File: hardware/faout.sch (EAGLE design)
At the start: 159 parts, among them IC2 MT48LC8M16A2, P1 TE_CONN_MTE_HEADER3R, Q1 L7812CD2T-TR, Q2 L7912CD2T-TR, Q3 12MHz, Q4 ASFL, U1 LM3671MF-3.3, U10 REF102AU, U11 OPA4277UA, U12 DAC8812, U13 REF102AU, U14 OPA4277UA, U15 DAC8812, U16 LM7321MF, U2 LM3671MF-1.2, U3 93LC46BT-I/OT, U4 6SLX9TQG144, U5 M25PE16SO8N, U7 REF102AU, U8 OPA4277UA, U9 DAC8812

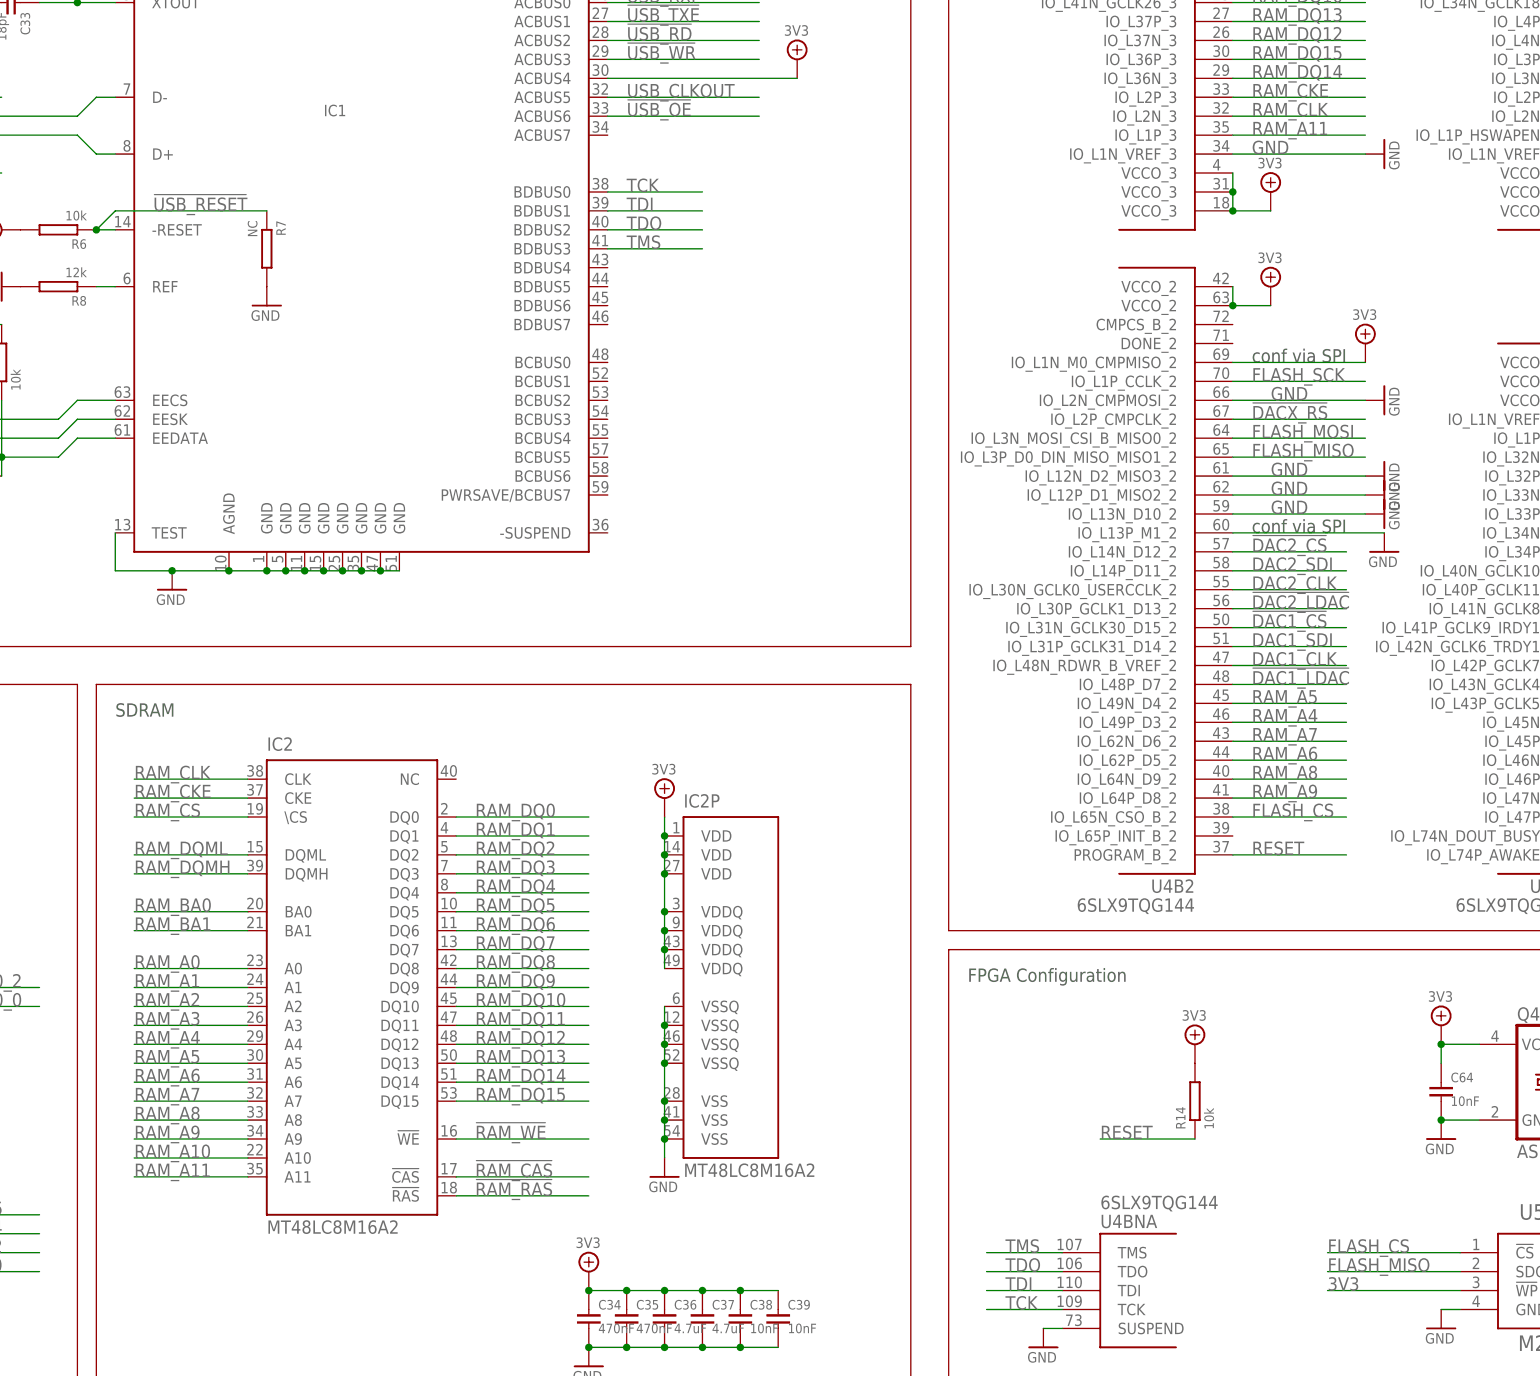
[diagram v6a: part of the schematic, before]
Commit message: Modify board for 256Mbit DRAM (MT48LC16M16) compatibility.
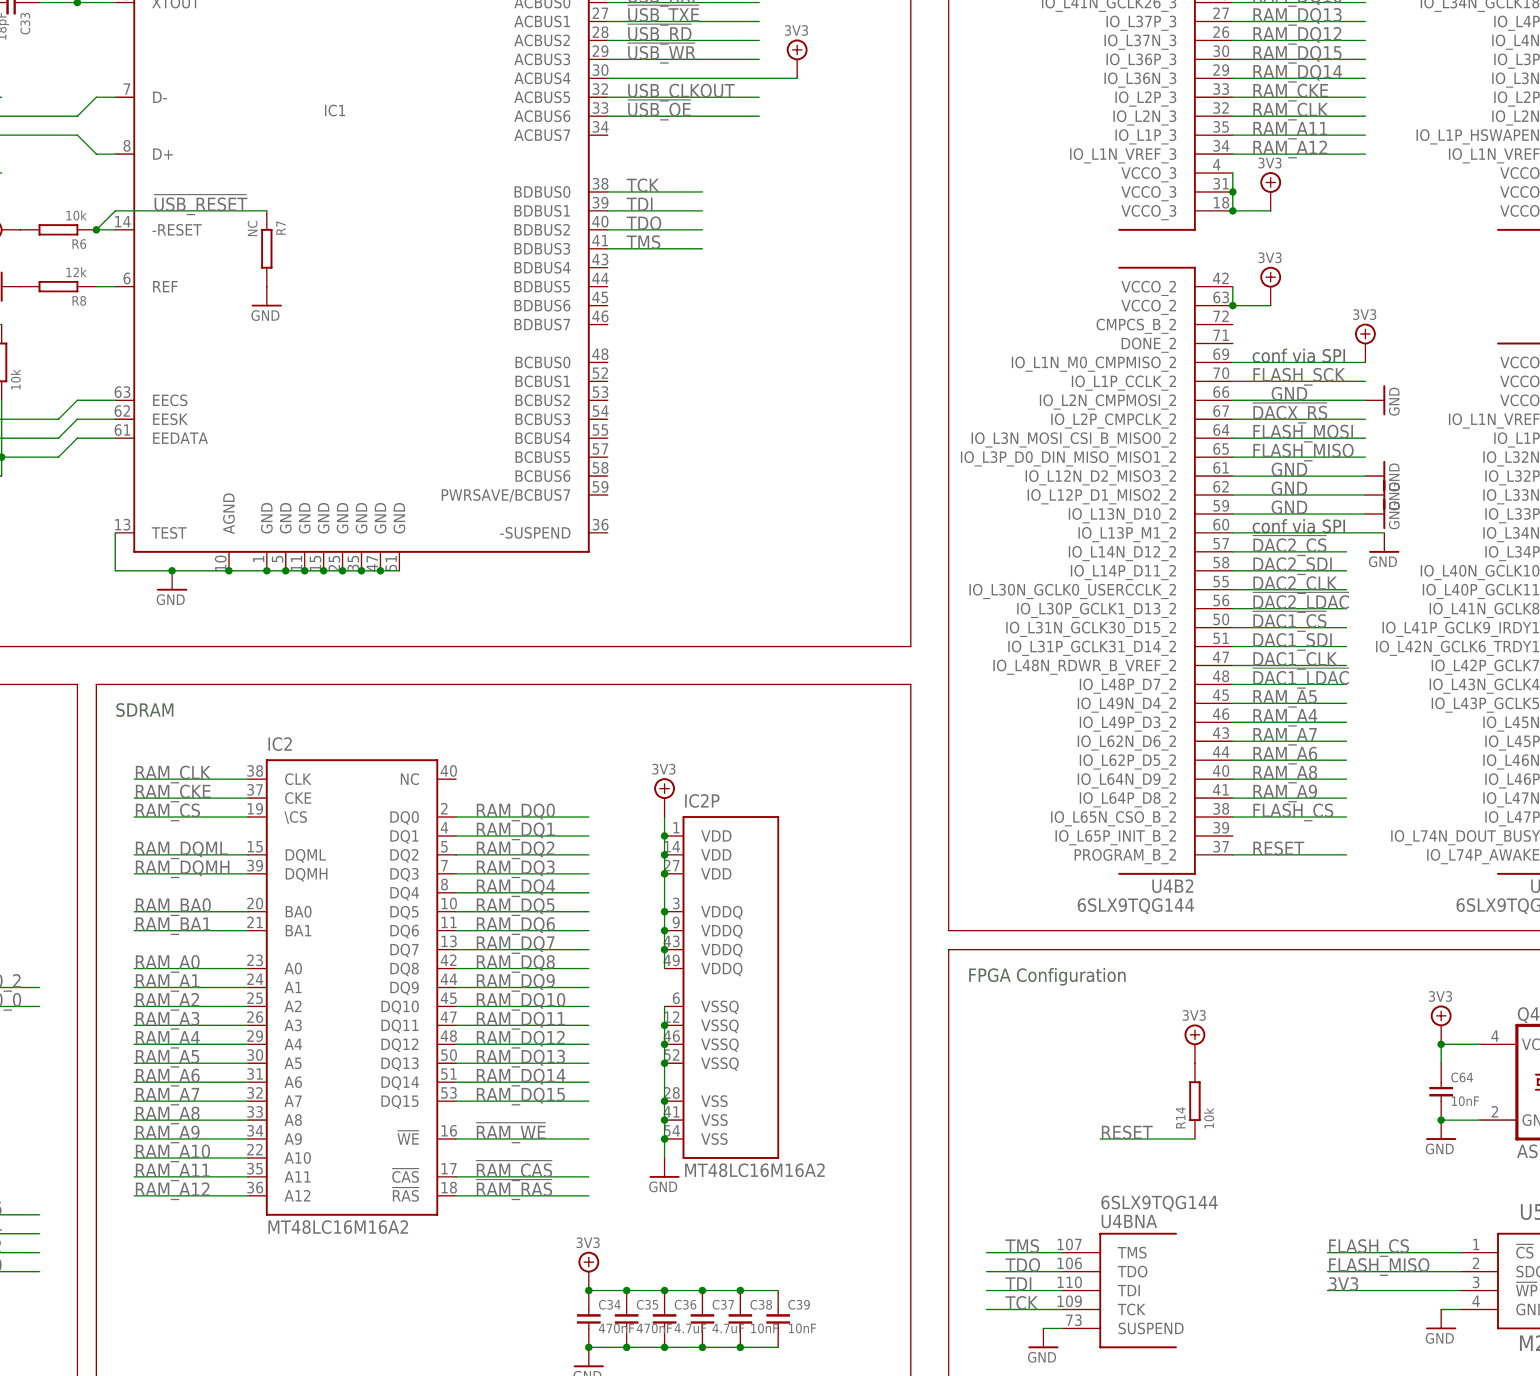
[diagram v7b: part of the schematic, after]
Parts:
- IC2: value MT48LC8M16A2 -> MT48LC16M16A2; device faout:MT48LC8M16A2 -> faout:MT48LC16M16A2
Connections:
- new net RAM_A12: IC2G$1.A12, U4B3.IO_L1N_VREF_3
- net GND: no longer U4B3.IO_L1N_VREF_3
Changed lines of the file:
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@@
 <attribute name="OC_FARNELL" value="1697461"/>
 </part>
-<part name="IC2" library="faout" deviceset="MT48LC" device="8M16A2"/>
+<part name="IC2" library="faout" deviceset="MT48LC" device="16M16A2" value="MT48LC16M16A2"/>
 <part name="3V3_PWR20" library="faout" deviceset="3V3" device=""/>
 <part name="3V3_PWR22" library="faout" deviceset="3V3" device=""/>
@@
 <part name="A+3V3_PWR10" library="faout" deviceset="A+3V3" device=""/>
 <part name="SUPPLY44" library="supply2" deviceset="AGND" device=""/>
-<part name="GND_PWR51" library="faout" deviceset="GND" device=""/>
 <part name="C73" library="faout" deviceset="C_EU" device="0603" value="10nF">
 <attribute name="OC_FARNELL" value="1759102"/>
@@
 <instance part="A+3V3_PWR10" gate="G$1" x="322.58" y="-269.24"/>
 <instance part="SUPPLY44" gate="G$1" x="322.58" y="-281.94"/>
-<instance part="GND_PWR51" gate="A" x="203.2" y="-129.54" rot="R90"/>
 <instance part="C73" gate="G$1" x="320.04" y="-274.32">
 <attribute name="OC_FARNELL" x="320.04" y="-274.32" size="1.778" layer="96" display="off"/>
@@
 <pinref part="U4" gate="B1" pin="IO_L40N_GCLK10_1"/>
 </segment>
-<segment>
-<pinref part="U4" gate="B3" pin="IO_L1N_VREF_3"/>
-<pinref part="GND_PWR51" gate="A" pin="GND"/>
-<wire x1="200.66" y1="-129.54" x2="182.88" y2="-129.54" width="0.1524" layer="91"/>
-<label x="185.42" y="-129.54" size="1.778" layer="95"/>
-</segment>
 </net>
 <net name="N$1" class="0">
@@
 </segment>
 </net>
+<net name="RAM_A12" class="0">
+<segment>
+<pinref part="U4" gate="B3" pin="IO_L1N_VREF_3"/>
+<wire x1="182.88" y1="-129.54" x2="200.66" y2="-129.54" width="0.1524" layer="91"/>
+<label x="185.42" y="-129.54" size="1.778" layer="95"/>
+</segment>
+<segment>
+<wire x1="35.56" y1="-269.24" x2="50.8" y2="-269.24" width="0.1524" layer="91"/>
+<label x="35.56" y="-269.24" size="1.778" layer="95"/>
+<pinref part="IC2" gate="G$1" pin="A12"/>
+</segment>
+</net>
